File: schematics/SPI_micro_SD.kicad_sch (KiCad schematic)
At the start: 1 part, among them J1 Micro_SD_Card

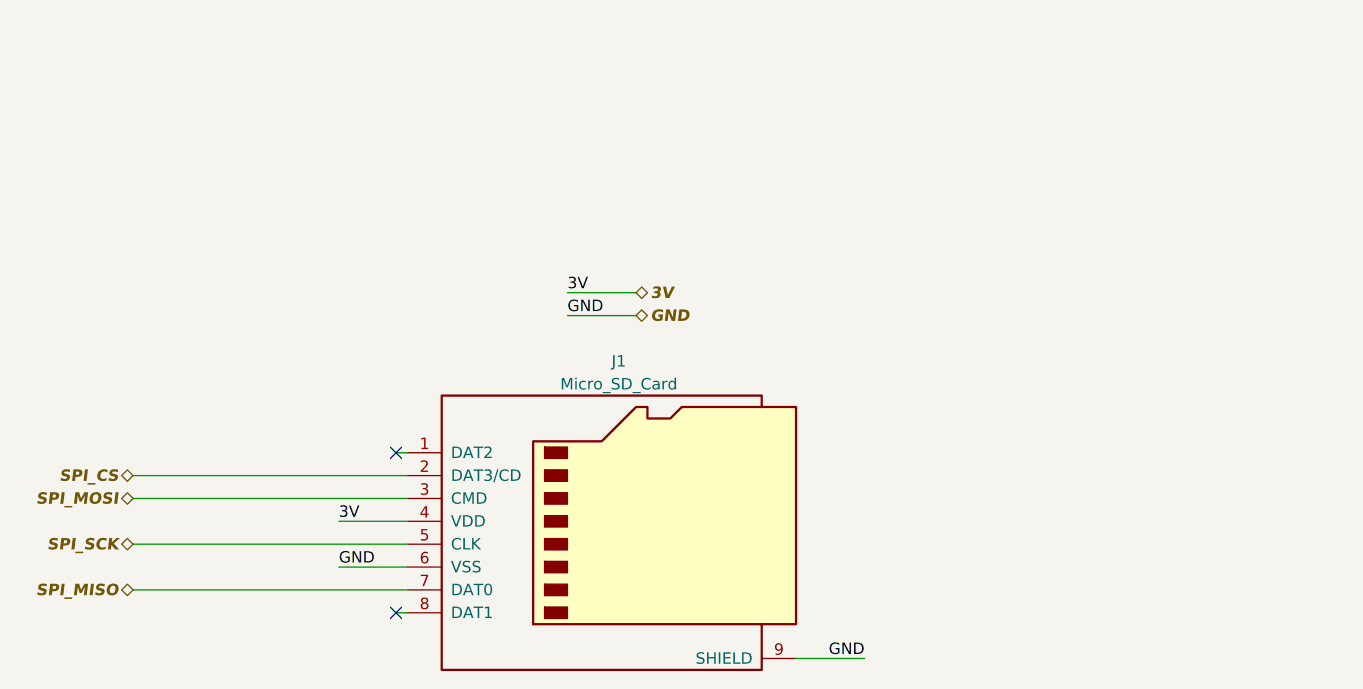
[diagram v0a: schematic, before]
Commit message: Обновил файлы и добавил новые элемнты
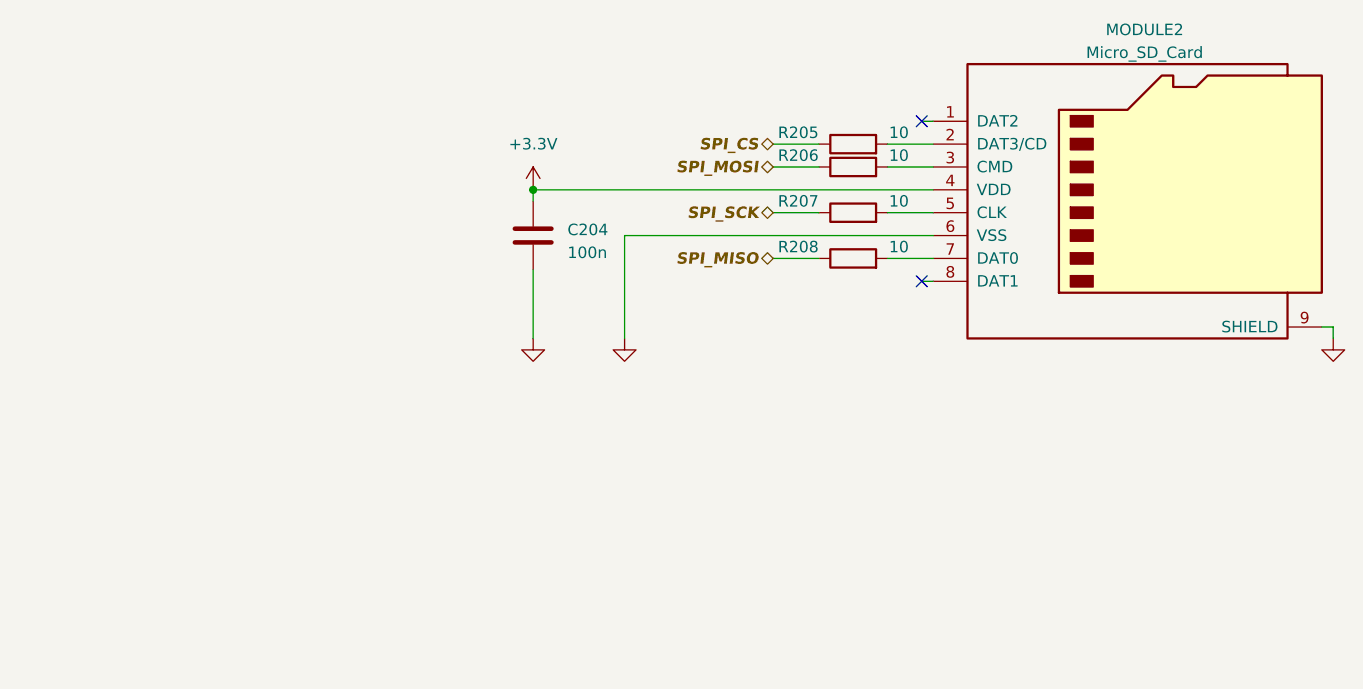
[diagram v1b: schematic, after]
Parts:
- added C204: 100n, Capacitor_SMD:C_1206_3216Metric_Pad1.33x1.80mm_HandSolder, symbol Device:C
- added R205, R206, R207, R208: 10, Resistor_SMD:R_1206_3216Metric_Pad1.30x1.75mm_HandSolder, symbol Device:R
- renumbered J1 to MODULE2
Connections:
- net GND: now also C204.1
- net SPI_CS: now also R205.1; no longer MODULE2.2 (DAT3/CD)
- net SPI_MISO: now also R208.1; no longer MODULE2.7 (DAT0)
- net SPI_MOSI: now also R206.1; no longer MODULE2.3 (CMD)
- net SPI_SCK: now also R207.1; no longer MODULE2.5 (CLK)
- net 3V renamed +3.3V
- net +3.3V: now also C204.2
- new net: MODULE2.3 (CMD), R206.2
- new net: MODULE2.5 (CLK), R207.2
- new net: MODULE2.2 (DAT3/CD), R205.2
- new net: MODULE2.7 (DAT0), R208.2
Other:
- moved on the sheet: MODULE2
